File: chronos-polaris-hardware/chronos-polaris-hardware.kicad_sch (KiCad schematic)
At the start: 35 parts, among them P1 WJ124-3_81-6P, U1 TPS62172DSGR, U10 MSK12C02-HB, U11 SS54_C22452, U12 AP20P30Q, U13 DMP2200UDW-7, U2 ESP32-S2, U3 BMI088, U4 BMP280, U5 TF_PUSH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

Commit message: checkpoint, mcu needs to be replaced
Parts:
- added H1, H2, H3, H4: MountingHole, symbol Mechanical:MountingHole
- added J1, J2, J3, J4, J5: Conn_01x03_Pin, Connector_PinHeader_2.54mm:PinHeader_1x03_P2.54mm_Vertical, symbol Connector:Conn_01x03_Pin
- added J6, J7: Conn_01x04, Connector_PinHeader_2.54mm:PinHeader_1x04_P2.54mm_Vertical, symbol Connector_Generic:Conn_01x04
- added J8: Conn_01x02, Connector_Wire:SolderWire-0.5sqmm_1x02_P4.6mm_D0.9mm_OD2.1mm, symbol Connector_Generic:Conn_01x02
- added R10, R9: 51, symbol Device:R
- added R11: 100, symbol Device:R
- added U14: FC-B1010RGBT-HG, polaris-fp:LED-ARRAY-SMD_4P-L1.0-W1.0-TR-RD, symbol polaris-sym:FC-B1010RGBT-HG
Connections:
- net 3.3V: now also R8.2, U2.1 (VDDA), U2.27 (VDD3P3_RTC_IO), U2.3 (VDD3P3), U2.4 (VDD3P3), U2.51 (VDDA), U2.54 (VDDA), J5.3 (Pin_3), J6.3 (Pin_3), U14.1 (+); no longer R8.1
- net 5V: now also U6.4 (FB), J1.2 (Pin_2), J2.2 (Pin_2), J3.2 (Pin_2), J4.2 (Pin_2), J5.2 (Pin_2)
- net BUZ_CTRL: now also U2.28 (GPIO21); no longer U2.13 (GPIO8)
- net GND: now also U2.55 (GPIO46), U2.57 (GND), J1.1 (Pin_1), J2.1 (Pin_1), J3.1 (Pin_1), J4.1 (Pin_1), J5.1 (Pin_1), J6.1 (Pin_1)
- net at U3.10 (SDO2), U3.15 (SDO1): now also U2.35 (SPIQ), U4.5 (SDO)
- net at U3.14 (CSB1): now also U2.33 (SPICS0); no longer U2.29 (SPICS1)
- net at U3.5 (CSB2): now also U2.29 (SPICS1); no longer U2.37 (GPIO33)
- net DROGUE DETECT: now reaches U13.3 (D2), U2.9 (GPIO4)
- net MAIN DETECT: now reaches U13.6 (D1), U2.8 (GPIO3)
- net at U4.2 (CSB): now also U2.37 (GPIO33); no longer U2.33 (SPICS0)
- net RESET: now reaches C5.1
- net RESET: now also R8.1, U2.56 (CHIP_PU), J8.2 (Pin_2); no longer R8.2
- net DROGUE CTRL: now reaches R4.1, U2.7 (GPIO2), U8.5 (G2)
- net MAIN CTRL: now reaches R5.2, U2.6 (GPIO1), U8.2 (G1)
- net at U2.10 (GPIO5): now also J1.3 (Pin_3)
- net at U2.11 (GPIO6): now also J2.3 (Pin_3)
- net at U2.12 (GPIO7): now also J3.3 (Pin_3)
- net at U2.14 (GPIO9): now also J6.4 (Pin_4)
- net at U2.15 (GPIO10): now also J6.2 (Pin_2)
- net at U2.16 (GPIO11): now also R9.2
- net at U2.17 (GPIO12): now also R10.2
- net at U2.18 (GPIO13): now also R11.2
- net at U2.21 (XTAL_32K_P): now also J7.4 (Pin_4)
- net at U2.22 (XTAL_32K_N): now also J7.3 (Pin_3)
- net at U2.23 (DAC_1): now also J7.2 (Pin_2)
- net at U2.24 (DAC_2): now also J7.1 (Pin_1)
- net GPIO0 (BOOTLOADER): now reaches U2.5 (GPIO0)
- net GPIO0 (BOOTLOADER): now also J8.1 (Pin_1)
- net APOGEE V+ renamed DROGUE V+
- new net: J4.3 (Pin_3), U2.13 (GPIO8)
- new net: R9.1, U14.4 (-)
- new net: R11.1, U14.2 (-)
- new net: R10.1, U14.3 (-)
- no-connect marks 20 -> 35
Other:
- note added: "GPIO 1 O - MAIN CTRL (3.3 = FIRE) GPIO 2 O - DROGUE CTRL (3.3 = FIRE) GPIO 3 I - MAIN DETECT (3.3 = CONNECTED) GPIO 4 I - DROGUE DETECT (3.3 = CONNECTED) GPIO 5,6,7,8 - SERVOS 1,2,3,4 GPIO 9 - [EXT] I2C SCL GPIO 10 - [EXT] I2C SDA GPIO 11,12,13 - LED PWM R,G,B (0 = ON) GPIO 15 - [EXT] SPI CS / XTAL_32K_P GPIO 16 - [EXT] SPI CLK / XTAL_32K_N GPIO 17 - [EXT] SPI MOSI / DAC1 / ADC GPIO 18 - [EXT] SP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"
- note removed: "GPIO 1 O - MAIN CTRL (3.3 = FIRE) GPIO 2 O - APOGEE CTRL (3.3 = FIRE) GPIO 3 I - MAIN DETECT (3.3 = CONNECTED) GPIO 4 I - APOGEE DETECT (3.3 = CONNECTED)"
- moved on the sheet: C4, C5, R8, USB1

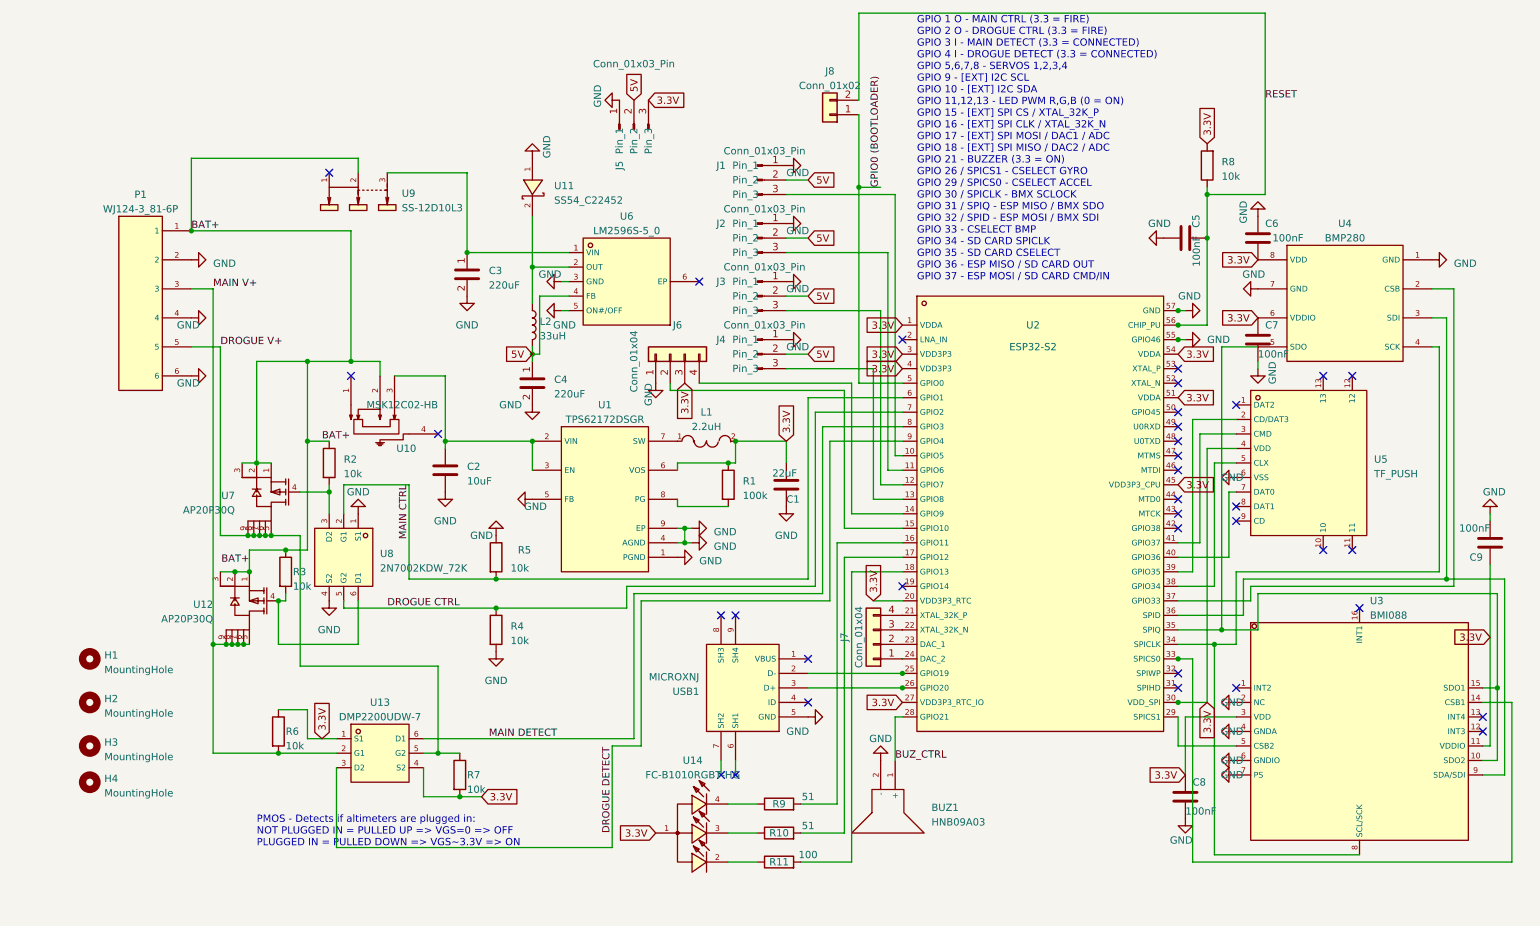
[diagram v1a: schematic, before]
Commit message: finish schematic for real, start pcb
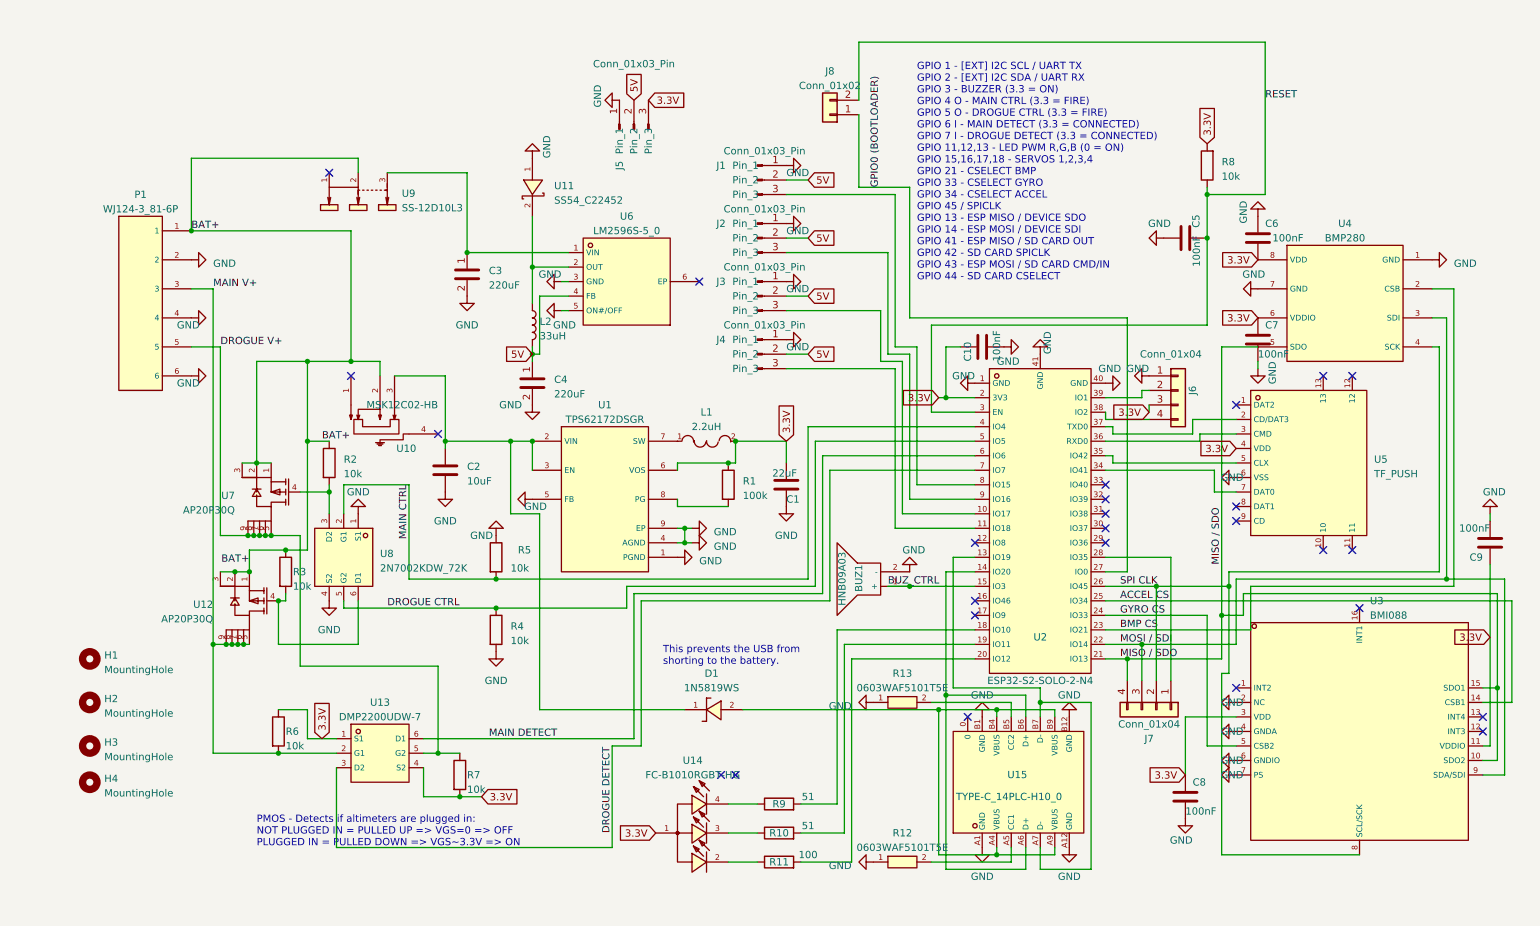
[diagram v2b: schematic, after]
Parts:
- removed U2: ESP32-S2, polaris-fp:QFN-56_L7.0-W7.0-P0.40-TL-EP4.0, symbol polaris-sym:ESP32-S2
- removed USB1: MICROXNJ, polaris-fp:MICRO-USB-SMD_MICROXNJ, symbol polaris-sym:MICROXNJ
- added C10: 100nF, Capacitor_SMD:C_0402_1005Metric, symbol Device:C
- added D1: 1N5819WS, polaris-fp:SOD-323_L1.8-W1.3-LS2.5-RD, symbol polaris-sym:1N5819WS
- added R12, R13: 0603WAF5101T5E, polaris-fp:R0603, symbol polaris-sym:0603WAF5101T5E
- added U15: TYPE-C_14PLC-H10_0, polaris-fp:USB-C-TH_SHOUHAN_TYPE-C-14PLC-H10.0, symbol polaris-sym:TYPE-C_14PLC-H10_0
- added U2: ESP32-S2-SOLO-2-N4, polaris-fp:WIRELM-SMD_ESP32-S3-WROOM-1, symbol polaris-sym:ESP32-S2-SOLO-2-N4
- C1: footprint (none) -> Capacitor_SMD:C_0603_1608Metric
- C2: footprint (none) -> Capacitor_SMD:C_0805_2012Metric
- C5, C6, C7, C8, C9: footprint (none) -> Capacitor_SMD:C_0402_1005Metric
- H1, H2, H3, H4: footprint (none) -> MountingHole:MountingHole_3.2mm_M3_Pad
- J8: footprint Connector_Wire:SolderWire-0.5sqmm_1x02_P4.6mm_D0.9mm_OD2.1mm -> Connector_PinHeader_2.54mm:PinHeader_1x02_P2.54mm_Vertical
- R1, R10, R11, R2, R3, R4, R5, R6, R7, R8, R9: footprint (none) -> Resistor_SMD:R_0603_1608Metric
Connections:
- net 3.3V: now also C10.1, U2.2 (3V3)
- net BUZ_CTRL: now also U2.15 (IO3)
- net DROGUE CTRL: now also U2.5 (IO5)
- net DROGUE DETECT: now also U2.7 (IO7)
- net GND: now also C10.2, R12.1, R13.1, U15.A1 (GND), U15.A12 (GND), U15.B1 (GND), U15.B12 (GND), U2.1 (GND), U2.40 (GND), U2.41 (GND)
- net GPIO0 (BOOTLOADER): now also U2.27 (IO0)
- net MAIN CTRL: now also U2.4 (IO4)
- net MAIN DETECT: now also U2.6 (IO6)
- net RESET: now also U2.3 (EN)
- net at J4.3 (Pin_3): now also U2.11 (IO18)
- net at J6.2 (Pin_2): now also U2.39 (IO1)
- net at J6.4 (Pin_4): now also U2.38 (IO2)
- net MISO / SDO: now reaches U3.10 (SDO2), U3.15 (SDO1), U4.5 (SDO)
- net MISO / SDO: now also J7.4 (Pin_4), U2.21 (IO13)
- net ACCEL CS: now reaches U3.14 (CSB1)
- net ACCEL CS: now also U2.25 (IO34)
- net GYRO CS: now reaches U3.5 (CSB2)
- net GYRO CS: now also U2.24 (IO33)
- net SPI CLK: now reaches U3.8 (SCL/SCK), U4.4 (SCK)
- net SPI CLK: now also J7.2 (Pin_2), U2.26 (IO45)
- net MOSI / SDI: now reaches U3.9 (SDA/SDI), U4.3 (SDI)
- net MOSI / SDI: now also J7.3 (Pin_3), U2.22 (IO14)
- net at R9.2: now also U2.18 (IO10)
- net at J2.3 (Pin_3): now also U2.9 (IO16)
- net at J3.3 (Pin_3): now also U2.10 (IO17)
- net BMP CS: now reaches U4.2 (CSB)
- net BMP CS: now also U2.23 (IO21)
- net at C2.1, U1.2 (VIN), U1.3 (EN)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: now also D1.1 (C)
- net at U5.2 (CD/DAT3): now also U2.37 (TXD0)
- net at U5.3 (CMD): now also U2.36 (RXD0)
- net at U5.5 (CLX): now also U2.35 (IO42)
- net at U5.7 (DAT0): now also U2.34 (IO41)
- net at J7.1 (Pin_1): now also U2.28 (IO35)
- net at J1.3 (Pin_3): now also U2.8 (IO15)
- net at R10.2: now also U2.19 (IO11)
- net at R11.2: now also U2.20 (IO12)
- new net: U15.A7 (D-), U15.B7 (D-), U2.13 (IO19)
- new net: U15.A6 (D+), U15.B6 (D+), U2.14 (IO20)
- new net: D1.2 (A), U15.A4 (VBUS), U15.A9 (VBUS), U15.B4 (VBUS), U15.B9 (VBUS)
- new net: R13.2, U15.B5 (CC2)
- new net: R12.2, U15.A5 (CC1)
- no-connect marks 35 -> 26
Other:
- note added: "GPIO 1 - [EXT] I2C SCL / UART TX GPIO 2 - [EXT] I2C SDA / UART RX GPIO 3 - BUZZER (3.3 = ON) GPIO 4 O - MAIN CTRL (3.3 = FIRE) GPIO 5 O - DROGUE CTRL (3.3 = FIRE) GPIO 6 I - MAIN DETECT (3.3 = CONNECTED) GPIO 7 I - DROGUE DETECT (3.3 = CONNECTED) GPIO 11,12,13 - LED PWM R,G,B (0 = ON) GPIO 15,16,17,18 - SERVOS 1,2,3,4 GPIO 21 - CSELECT BMP GPIO 33 - CSELECT GYRO GPIO 34 - CSELECT ACCEL GPIO 45 / 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"
- note added: "This prevents the USB from shorting to the battery."
- note removed: "GPIO 1 O - MAIN CTRL (3.3 = FIRE) GPIO 2 O - DROGUE CTRL (3.3 = FIRE) GPIO 3 I - MAIN DETECT (3.3 = CONNECTED) GPIO 4 I - DROGUE DETECT (3.3 = CONNECTED) GPIO 5,6,7,8 - SERVOS 1,2,3,4 GPIO 9 - [EXT] I2C SCL GPIO 10 - [EXT] I2C SDA GPIO 11,12,13 - LED PWM R,G,B (0 = ON) GPIO 15 - [EXT] SPI CS / XTAL_32K_P GPIO 16 - [EXT] SPI CLK / XTAL_32K_N GPIO 17 - [EXT] SPI MOSI / DAC1 / ADC GPIO 18 - [EXT] SP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"
- moved on the sheet: BUZ1, J6

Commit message: convert ematch detect to voltage divider
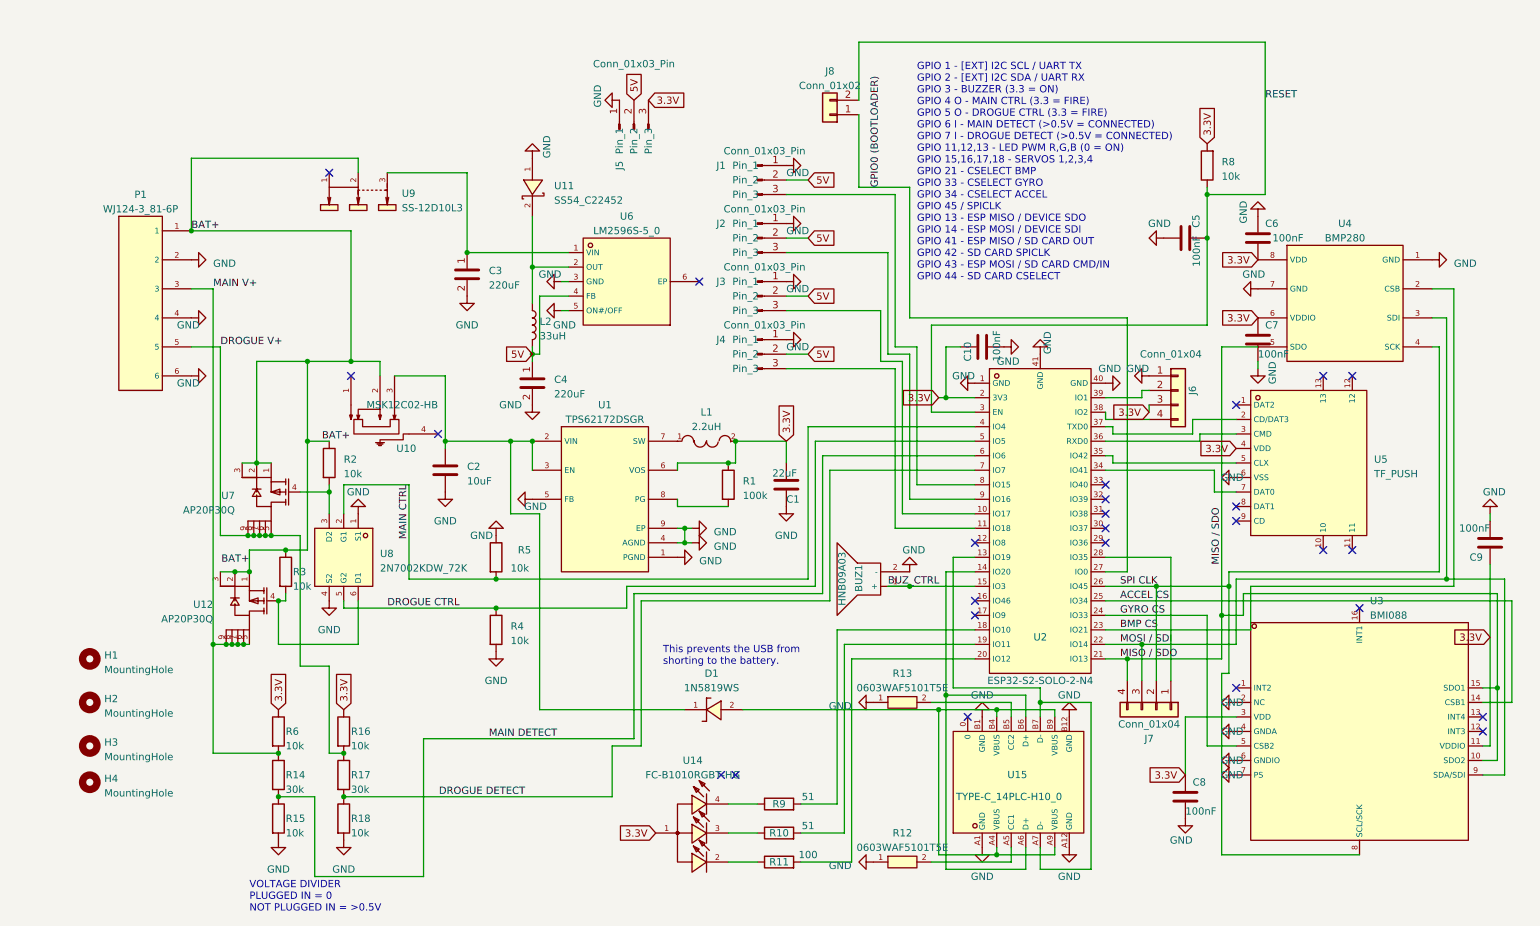
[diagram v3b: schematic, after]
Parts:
- removed R7: 10k, Resistor_SMD:R_0603_1608Metric, symbol Device:R
- removed U13: DMP2200UDW-7, polaris-fp:SOT-363_L2.0-W1.3-P0.65-LS2.1-BL, symbol polaris-sym:DMP2200UDW-7
- added R14, R17: 30k, Resistor_SMD:R_0603_1608Metric, symbol Device:R
- added R15, R16, R18: 10k, Resistor_SMD:R_0603_1608Metric, symbol Device:R
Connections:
- net 3.3V: now also R16.1
- net DROGUE DETECT: now also R17.2, R18.1
- net DROGUE V+: now also R16.2, R17.1
- net GND: now also R15.2, R18.2
- net MAIN DETECT: now also R14.2, R15.1
- net MAIN V+: now also R14.1
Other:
- note added: "GPIO 1 - [EXT] I2C SCL / UART TX GPIO 2 - [EXT] I2C SDA / UART RX GPIO 3 - BUZZER (3.3 = ON) GPIO 4 O - MAIN CTRL (3.3 = FIRE) GPIO 5 O - DROGUE CTRL (3.3 = FIRE) GPIO 6 I - MAIN DETECT (>0.5V = CONNECTED) GPIO 7 I - DROGUE DETECT (>0.5V = CONNECTED) GPIO 11,12,13 - LED PWM R,G,B (0 = ON) GPIO 15,16,17,18 - SERVOS 1,2,3,4 GPIO 21 - CSELECT BMP GPIO 33 - CSELECT GYRO GPIO 34 - CSELECT ACCEL GPIO 4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"
- note added: "VOLTAGE DIVIDER PLUGGED IN = 0 NOT PLUGGED IN = >0.5V"
- note removed: "GPIO 1 - [EXT] I2C SCL / UART TX GPIO 2 - [EXT] I2C SDA / UART RX GPIO 3 - BUZZER (3.3 = ON) GPIO 4 O - MAIN CTRL (3.3 = FIRE) GPIO 5 O - DROGUE CTRL (3.3 = FIRE) GPIO 6 I - MAIN DETECT (3.3 = CONNECTED) GPIO 7 I - DROGUE DETECT (3.3 = CONNECTED) GPIO 11,12,13 - LED PWM R,G,B (0 = ON) GPIO 15,16,17,18 - SERVOS 1,2,3,4 GPIO 21 - CSELECT BMP GPIO 33 - CSELECT GYRO GPIO 34 - CSELECT ACCEL GPIO 45 / 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"
- note removed: "PMOS - Detects if altimeters are plugged in: NOT PLUGGED IN = PULLED UP => VGS=0 => OFF PLUGGED IN = PULLED DOWN => VGS~3.3V => ON"

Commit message: finish PCB layout
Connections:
- net at R9.2: now also U2.35 (IO42); no longer U2.18 (IO10)
- net at U2.17 (IO9): now also U5.7 (DAT0)
- net at U2.19 (IO11): now also U5.3 (CMD); no longer R10.2
- net at U2.20 (IO12): now also U5.2 (CD/DAT3); no longer R11.2
- net at U2.34 (IO41): no longer U5.7 (DAT0)
- net at U5.5 (CLX): now also U2.18 (IO10); no longer U2.35 (IO42)
- net at U2.36 (RXD0): now also R10.2; no longer U5.3 (CMD)
- net at U2.37 (TXD0): now also R11.2; no longer U5.2 (CD/DAT3)
- no-connect marks 26 -> 24
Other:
- note added: "GPIO 1 - [EXT] I2C SCL / UART TX GPIO 2 - [EXT] I2C SDA / UART RX GPIO 3 - BUZZER (3.3 = ON) GPIO 4 O - MAIN CTRL (3.3 = FIRE) GPIO 5 O - DROGUE CTRL (3.3 = FIRE) GPIO 6 I - MAIN DETECT (>0.5V = CONNECTED) GPIO 7 I - DROGUE DETECT (>0.5V = CONNECTED) GPIO 9 - ESP MISO / SD CARD DATA OUT GPIO 10 - SD CARD SPICLK GPIO 11 - ESP MOSI / SD CARD CMD/IN GPIO 12 - SD CARD CSELECT GPIO 15,16,17,18 - SERVO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"
- note removed: "GPIO 1 - [EXT] I2C SCL / UART TX GPIO 2 - [EXT] I2C SDA / UART RX GPIO 3 - BUZZER (3.3 = ON) GPIO 4 O - MAIN CTRL (3.3 = FIRE) GPIO 5 O - DROGUE CTRL (3.3 = FIRE) GPIO 6 I - MAIN DETECT (>0.5V = CONNECTED) GPIO 7 I - DROGUE DETECT (>0.5V = CONNECTED) GPIO 11,12,13 - LED PWM R,G,B (0 = ON) GPIO 15,16,17,18 - SERVOS 1,2,3,4 GPIO 21 - CSELECT BMP GPIO 33 - CSELECT GYRO GPIO 34 - CSELECT ACCEL GPIO 4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"
- moved on the sheet: R10, R11, R9, U14, U5

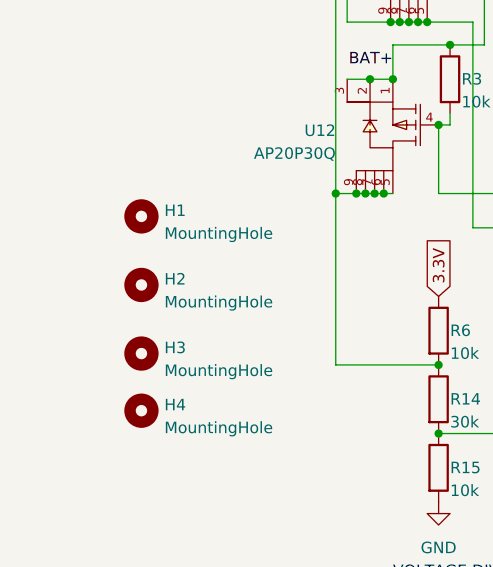
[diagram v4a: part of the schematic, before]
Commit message: improve ground planes
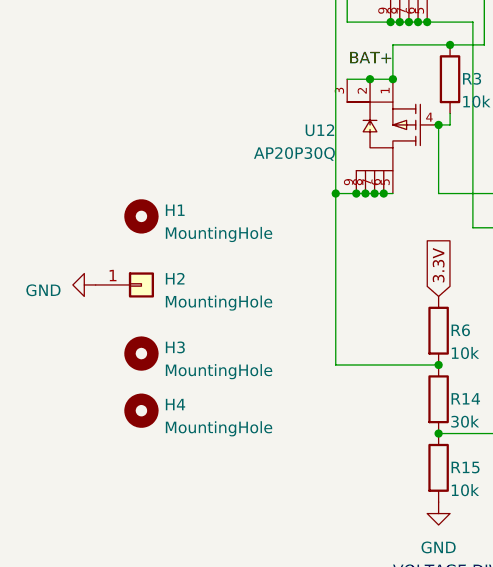
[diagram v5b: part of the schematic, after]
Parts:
- H2: symbol Mechanical:MountingHole -> Connector_Generic:Conn_01x01
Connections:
- net GND: now also H2.1 (Pin_1)
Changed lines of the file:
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@@
+    )
+  )
+  (symbol (lib_id "power:GND") (at 30.48 135.89 270) (unit 1)
+    (in_bom yes) (on_board yes) (dnp no) (fields_autoplaced)
+    (property "Reference" "#PWR050" (at 24.13 135.89 0)
+      (effects (font (size 1.27 1.27)) hide)
+    )
+    (property "Value" "GND" (at 26.67 136.525 90)
+      (effects (font (size 1.27 1.27)) (justify right))
+    )
+    (property "Footprint" "" (at 30.48 135.89 0)
+      (effects (font (size 1.27 1.27)) hide)
+    )
+    (property "Datasheet" "" (at 30.48 135.89 0)
+      (effects (font (size 1.27 1.27)) hide)
+    )
+    (pin "1")
+    (instances
+      (project "chronos-polaris-hardware"
+        (path "/503f01d5-a0c6-4ade-b485-97c3c2e1d6c5"
+          (reference "#PWR050") (unit 1)
+        )
+      )
     )
   )
@@
     )
   )
-  (symbol (lib_id "Mechanical:MountingHole") (at 35.56 135.89 0) (unit 1)
-    (in_bom yes) (on_board yes) (dnp no) (fields_autoplaced)
+  (symbol (lib_id "Connector_Generic:Conn_01x01") (at 35.56 135.89 0) (unit 1)
+    (in_bom yes) (on_board yes) (dnp no)
     (property "Reference" "H2" (at 38.1 135.255 0)
       (effects (font (size 1.27 1.27)) (justify left))
@@
       (effects (font (size 1.27 1.27)) hide)
     )
-    (instances
-      (project "chronos-polaris-hardware"
+    (pin "1")
+    (instances
+      (project "chronos-polaris-hardware"
